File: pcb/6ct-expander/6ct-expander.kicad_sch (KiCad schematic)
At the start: 3 parts, among them J7 Conn_02x05_Odd_Even

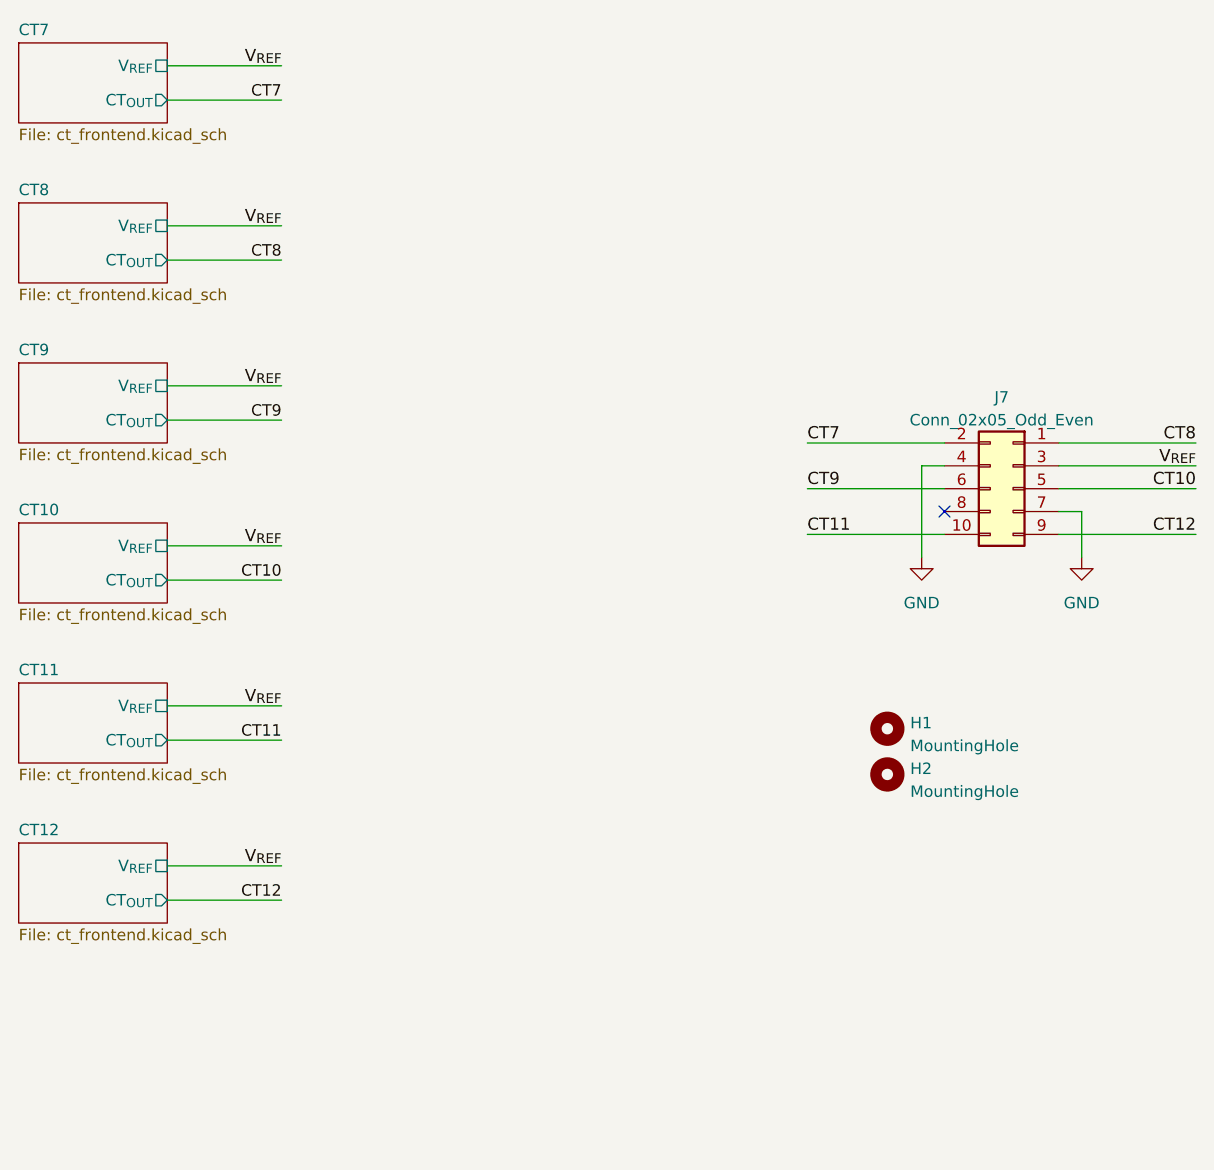
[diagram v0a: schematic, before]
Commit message: [6CT] Correct header, add extra GND pads
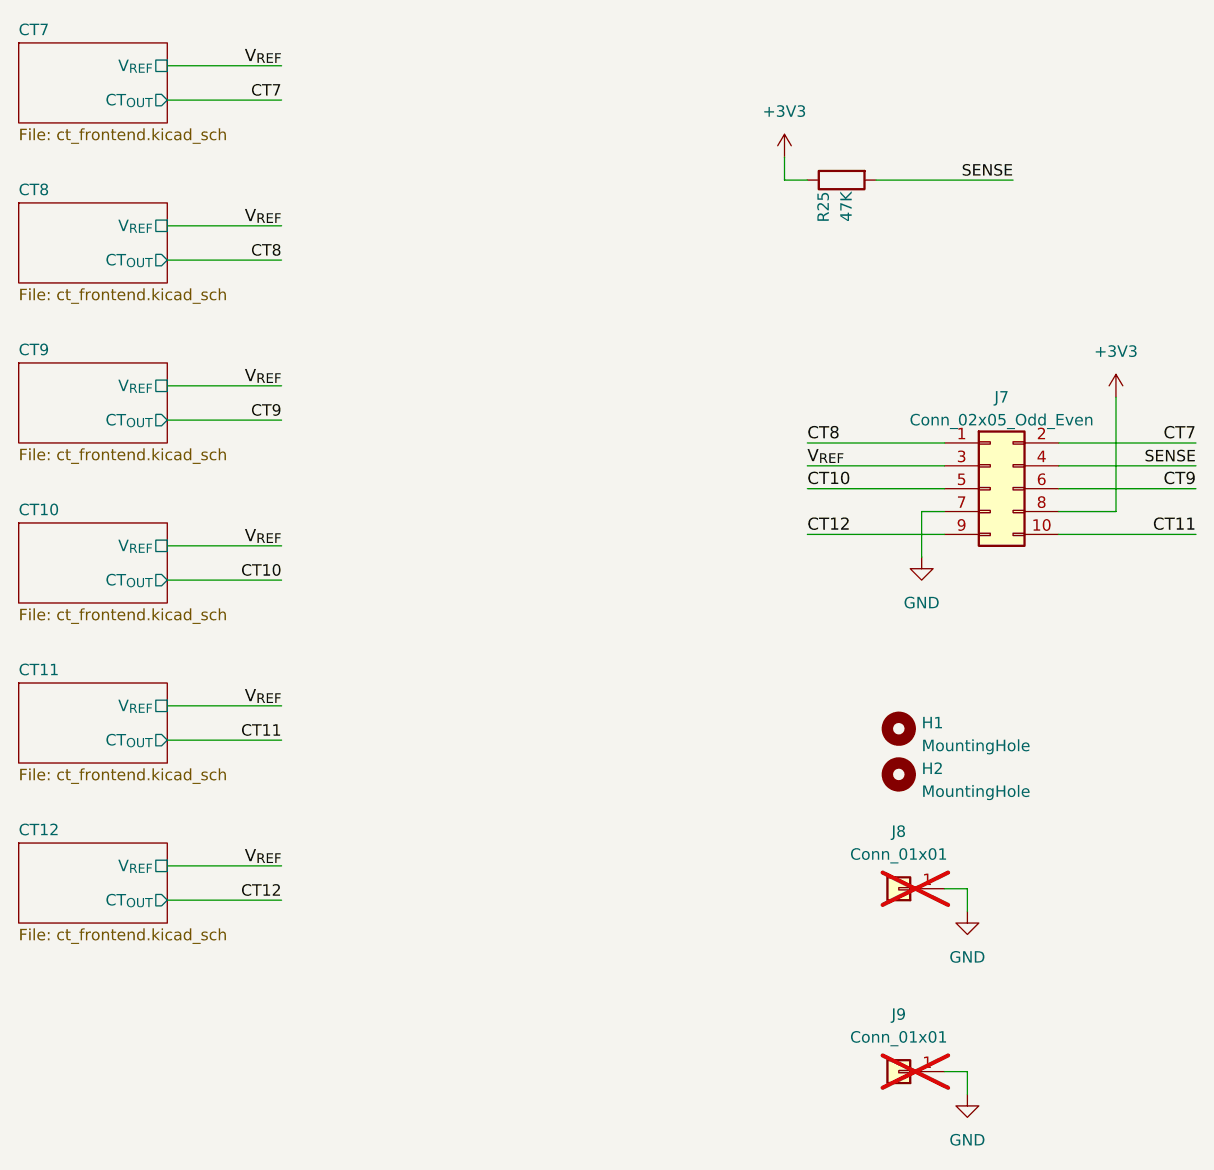
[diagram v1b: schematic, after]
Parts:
- added J8, J9: Conn_01x01, Connector_PinHeader_2.54mm:PinHeader_1x01_P2.54mm_Vertical, symbol Connector_Generic:Conn_01x01
- added R25: 47K, Resistor_SMD:R_0603_1608Metric, symbol Device:R
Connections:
- net GND: now also J8.1 (Pin_1), J9.1 (Pin_1); no longer J7.4 (Pin_4)
- net +3V3: now reaches J7.8 (Pin_8)
- net +3V3: now also R25.1
- new net SENSE: J7.4 (Pin_4), R25.2
- no-connect marks 1 -> 0
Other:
- title: emonPi3 / Tx6 6CT expander -> CT Expander
- moved on the sheet: H1, H2
